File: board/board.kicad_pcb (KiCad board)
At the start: 2 copper layers, 44.4 x 63.5 mm, 68 parts, among them J1 Screw_Terminal_01x02, J2 USB_B_Micro, J3 Screw_Terminal_01x02, J5 Conn_02x03_Odd_Even, J6 Conn_01x02_Male, Q1 Q_NJFET_GSD, Q2 Q_NJFET_GSD, Q3 Q_NJFET_GSD, Q4 Q_NJFET_GSD, SW1 SW_SPDT, SW2 SW_SPDT, SW3 SW_DIP_x01, U1 XBee, U2 ATxmega128A4U-AU, U3 FT230XS, U4 IC_REG_BCK_3.3V, U5 IC_REG_BOOST_ADJ_1.4A

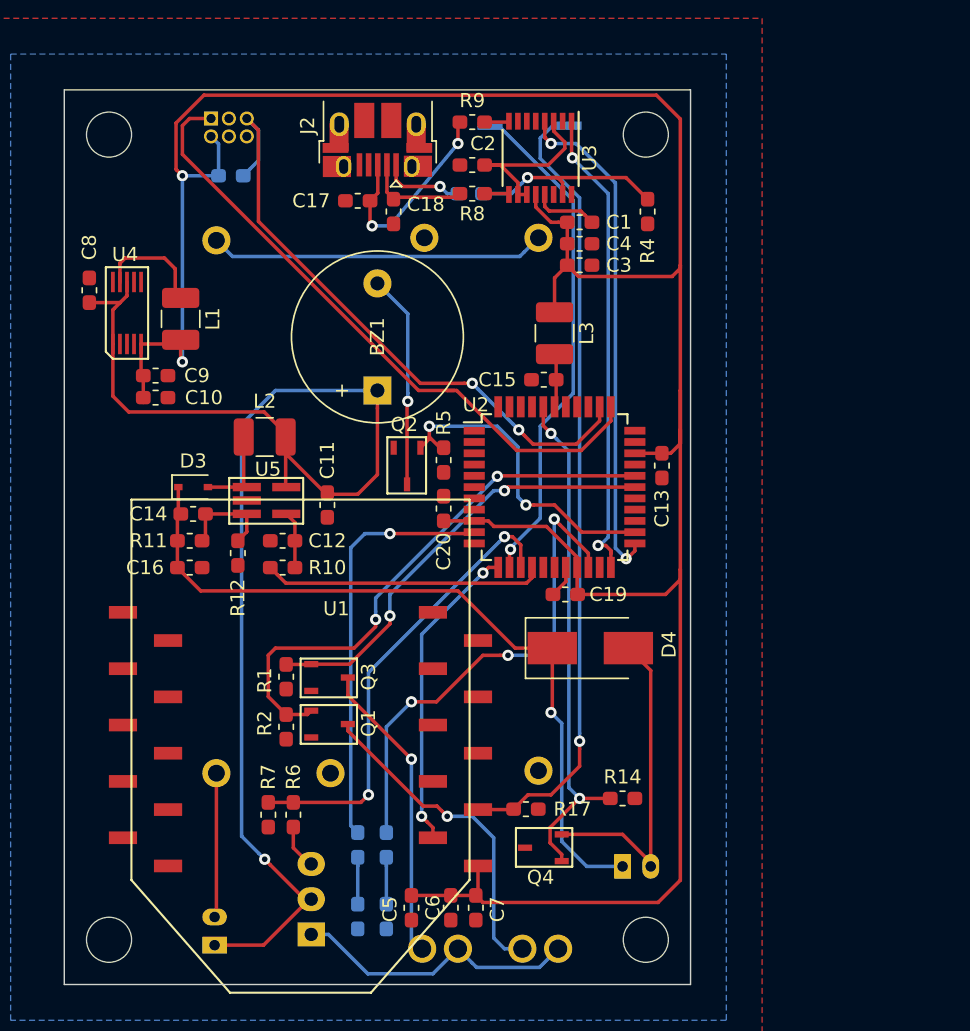
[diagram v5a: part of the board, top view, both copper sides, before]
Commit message: Diode, MOSFET, 3-pin JST plug fixes
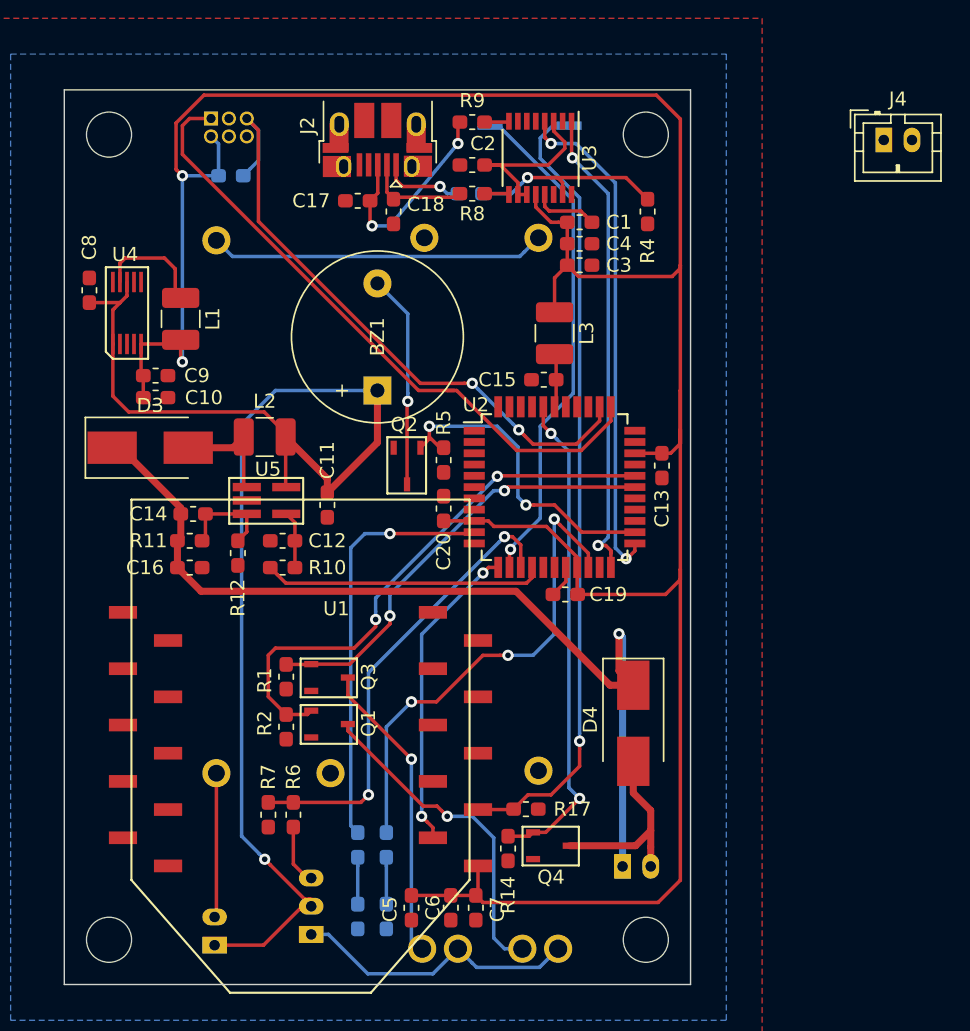
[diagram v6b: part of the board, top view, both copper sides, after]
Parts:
- added J4: Conn_01x02_Male, Connector_JST:JST_PH_B2B-PH-K_1x02_P2.00mm_Vertical, F.Cu at (115.3, 67.1)
- C12: value C_Small -> 1uF
- D3: footprint Diode_SMD:D_SOD-323 -> Diode_SMD:D_SMB_Handsoldering
- R10: value R_Small -> 10k
- SW1: footprint Connector_JST:JST_EH_B03B-EH-A_1x03_P2.50mm_Vertical -> Connector_JST:JST_PH_B3B-PH-K_1x03_P2.00mm_Vertical
- moved R14 8.87 mm to (88.6, 117.3), turned to 270 degrees
- moved Q4 6.19 mm to (90.4, 114.3), turned to 0 degrees
- moved D4 6.14 mm to (97.5, 108.5), turned to 270 degrees
- moved D3 4.13 mm to (63.2, 88.9)
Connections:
- Q4 pad 2: Net-(D4-Pad2) -> GND
- Q4 pad 3: GND -> Net-(D4-Pad2)
- R14 pad 1: GND -> /SOLENOID_CTRL
- R14 pad 2: /SOLENOID_CTRL -> GND
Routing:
- net +12V: track 54.0 -> 68.1 mm
- net Net-(D4-Pad2): track 23.6 -> 14.4 mm
- net Net-(D3-Pad2): track 6.66 -> 9.23 mm
- net /SOLENOID_CTRL: track 36.7 -> 35.1 mm
- net Net-(R6-Pad1): track 3.22 -> 4.31 mm
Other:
- net class High-current added: clearance 0.2, trace_width 0.5, via_dia 0.8, via_drill 0.4

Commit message: Fixed PCB for rev2
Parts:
- removed C1, C2, C3: 100nF, Capacitor_SMD:C_0603_1608Metric_Pad1.05x0.95mm_HandSolder
- removed C17, C18: 47pF, Capacitor_SMD:C_0603_1608Metric_Pad1.05x0.95mm_HandSolder
- removed C4: 4.7uF, Capacitor_SMD:C_0603_1608Metric_Pad1.05x0.95mm_HandSolder
- removed J2: USB_B_Micro, Connector_USB:USB_Micro-B_Amphenol_10103594-0001LF_Horizontal
- removed R8, R9: 27, Resistor_SMD:R_0603_1608Metric_Pad1.05x0.95mm_HandSolder
- removed U3: FT230XS, Package_SO:SSOP-16_3.9x4.9mm_P0.635mm
- added Q5: Q_NJFET_GSD, custom_components:NFET Toshiba SSM3K339R, F.Cu at (74.7, 99.1)
- added Q6: Q_PJFET_GSD, Package_TO_SOT_SMD:SOT-23_Handsoldering, F.Cu at (59.9, 95.2)
- BZ1: footprint Buzzer_Beeper:Buzzer_12x9.5RM7.6 -> custom_components:Buzzer_12x9.5RM7.6
- J4: footprint Connector_JST:JST_PH_B2B-PH-K_1x02_P2.00mm_Vertical -> Connector_Molex:Molex_MicroClasp_55932-0210_1x02_P2.00mm_Vertical; moved to B.Cu
- J5, R15, R16, SW3: moved to F.Cu
- J6, SW2: footprint Connector_JST:JST_PH_B2B-PH-K_1x02_P2.00mm_Vertical -> Connector_Molex:Molex_MicroClasp_55932-0210_1x02_P2.00mm_Vertical
- R3: value 47k -> 10K; moved to F.Cu
- SW1: footprint Connector_JST:JST_PH_B3B-PH-K_1x03_P2.00mm_Vertical -> Connector_Molex:Molex_MicroClasp_55932-0310_1x03_P2.00mm_Vertical
- moved J6 53.0 mm to (87.1, 66.5)
- moved R14 45.2 mm to (96.8, 72.9)
- moved Q4 40.7 mm to (91.4, 73.7), turned to 90 degrees
- moved J4 40.1 mm to (75.2, 66.5)
- moved R4 37.9 mm to (66.3, 91.9), turned to 180 degrees
- moved D4 36.9 mm to (86.9, 73.2)
- moved R3 33.7 mm to (72.9, 102.0), turned to 90 degrees
- moved R15 20.3 mm to (96.0, 112.8), turned to 270 degrees
- moved R16 20.1 mm to (97.8, 112.8), turned to 270 degrees
- moved D1 18.0 mm to (96.0, 117.6)
- moved D2 17.8 mm to (97.8, 117.6)
- moved SW3 15.9 mm to (96.8, 80.5), turned to 270 degrees
- moved J5 1.14 mm to (67.1, 66.5), turned to 90 degrees
- moved SW1 0.76 mm to (75.4, 123.4)
- moved Q3 0.51 mm to (74.7, 102.9)
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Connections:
- C14 pad 1: +12V -> Net-(C14-Pad1)
- C16 pad 1: +12V -> Net-(C14-Pad1)
- D3 pad 1: +12V -> Net-(C14-Pad1)
- R11 pad 1: +12V -> Net-(C14-Pad1)
- R3 pad 1: Net-(J2-Pad1) -> GND
- R3 pad 2: /VBUS_SENSE -> /LATCH_ENABLE
- R4 pad 1: /VBUS_SENSE -> Net-(Q5-Pad2)
- R4 pad 2: GND -> Net-(C14-Pad1)
- U2 pad 24: /BUZZER_CTRL -> Net-(U2-Pad24)
- U2 pad 28: /E_Match_Fire_1 -> /BUZZER_CTRL
- U2 pad 29: /E_Match_Fire_2 -> Net-(U2-Pad29)
- U2 pad 41: Net-(U2-Pad41) -> /E_Match_Fire_1
- U2 pad 42: Net-(U2-Pad42) -> /E_Match_Fire_2
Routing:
- net /USARTD0_TX: track 35.9 -> 0.00 mm, vias 2 -> 0
- net /USARTD0_RX: track 33.8 -> 0.00 mm, vias 2 -> 0
- net Net-(Q5-Pad2): track 0.00 -> 27.9 mm, vias 0 -> 3
- net Net-(C14-Pad1): track 0.00 -> 17.1 mm
- net Net-(R17-Pad1): track 56.6 -> 39.7 mm, vias 1 -> 2
- net /USB_D+: track 15.0 -> 0.00 mm, vias 2 -> 0
- net /VBUS_SENSE: track 14.6 -> 0.00 mm, vias 1 -> 0
- net /SOLENOID_CTRL: track 35.1 -> 20.8 mm
- net /FTDI_DECOUPLED_V: track 12.8 -> 0.00 mm
- net /LED2CTRL: track 34.7 -> 22.0 mm, vias 3 -> 1
- net /USARTC0_TX: track 36.0 -> 25.2 mm, vias 1 -> 2
- net /USB_D-: track 7.38 -> 0.00 mm
- net Net-(J2-Pad1): track 5.87 -> 0.00 mm, vias 1 -> 0
- net GND: track 7.73 -> 2.30 mm
- net /LATCH_ENABLE: track 19.9 -> 24.6 mm
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
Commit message: Software updates for hardware rev2
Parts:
- moved SW2 2.81 mm to (68.1, 121.4), turned to 270 degrees
- moved J1 0.76 mm to (84.6, 124.5)
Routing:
- net Net-(BT1-Pad1): track 10.3 -> 12.7 mm
- net +6V: track 100.1 -> 98.7 mm
- net Net-(BZ1-Pad2): track 15.2 -> 14.1 mm
- net Net-(J1-Pad2): track 21.3 -> 20.2 mm
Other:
- board text added: "CAP"
- board text added: "DETECT"
- board text added: "FIRE 1"
- board text added: "FIRE 2"
- board text added: "LATCH"
- board text added: "PWR SW"
- board text added: "UAH CRW 2019"
